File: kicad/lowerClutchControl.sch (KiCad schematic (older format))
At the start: 12 parts

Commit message: KICAD: Guardar cambios sch de los controles de los cluches y freno
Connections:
- net lowerClutchControl: now reaches J70.2 (Pin_2), Q13.2 (D), R32.2
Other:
- note added: "Blanco/Naranja"
- note added: "Naranja"
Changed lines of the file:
@@
 Sheet 17 22
 Title "Mainet-mega -- lowerClutchControl"
-Date "2021-04-07"
+Date "2021-07-09"
 Rev "1.0"
 Comp "Tovenca"
@@
 Text Label 7800 4300 0    50   ~ 0
 0V
+Text Label 7250 3150 0    50   ~ 0
+lowerClutchControl
+Text Notes 8350 3050 0    50   ~ 0
+Naranja
+Text Notes 8350 3250 0    50   ~ 0
+Blanco/Naranja
 $EndSCHEMATC

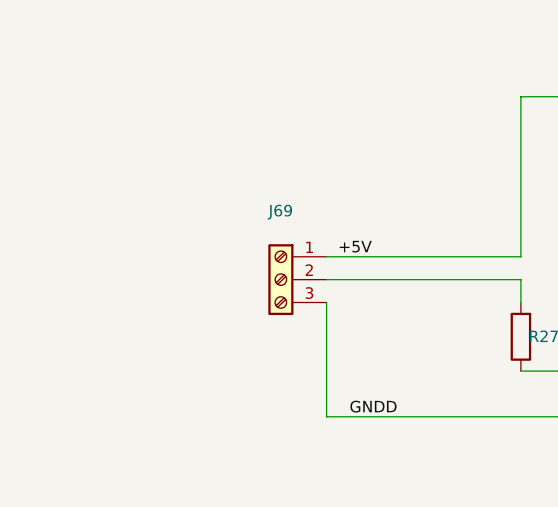
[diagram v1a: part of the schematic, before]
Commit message: KICAD: Agregar cvambios .sch controles tarjetas MP
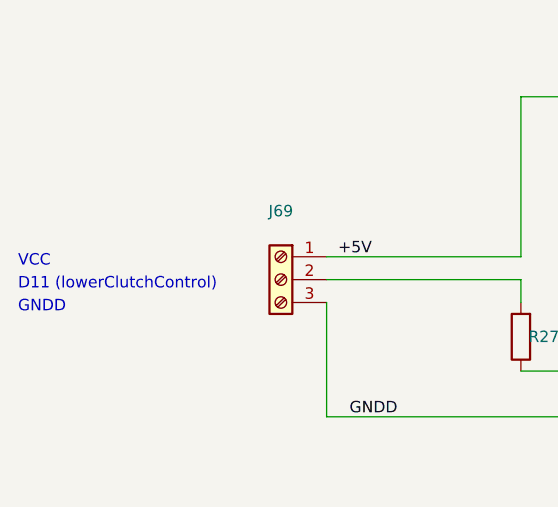
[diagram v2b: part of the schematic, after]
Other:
- note added: "D11 (lowerClutchControl)"
- note added: "GNDD"
- note added: "VCC"
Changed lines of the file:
@@
 Sheet 17 22
 Title "Mainet-mega -- lowerClutchControl"
-Date "2021-07-09"
+Date "2021-07-13"
 Rev "1.0"
 Comp "Tovenca"
@@
 Text Notes 8350 3250 0    50   ~ 0
 Blanco/Naranja
+Text Notes 2650 3450 0    50   ~ 0
+D11 (lowerClutchControl)
+Text Notes 2650 3550 0    50   ~ 0
+GNDD
+Text Notes 2650 3350 0    50   ~ 0
+VCC
 $EndSCHEMATC
